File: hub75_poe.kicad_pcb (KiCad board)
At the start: 4 copper layers, 70.5 x 48.3 mm, 103 parts, among them J1 0826-1X1T-JK-F, J2 Conn_02x08_Odd_Even, J3 7466003R, J4 502382-0970, J5 7466003R, Q1 FDS2582, SW1 434133025816, T1 PA2369NL, U1 KSZ8081MLX, U10 SN74LVC8T245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

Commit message: Add transformer snubber diode
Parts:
- added D12: BAS16W, Package_TO_SOT_SMD:SOT-323_SC-70, B.Cu at (131.1, 97.3)
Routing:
- net Net-(D12-Pad1): vias 0 -> 4
- added copper zone on B.Cu, net Net-(D12-Pad1)

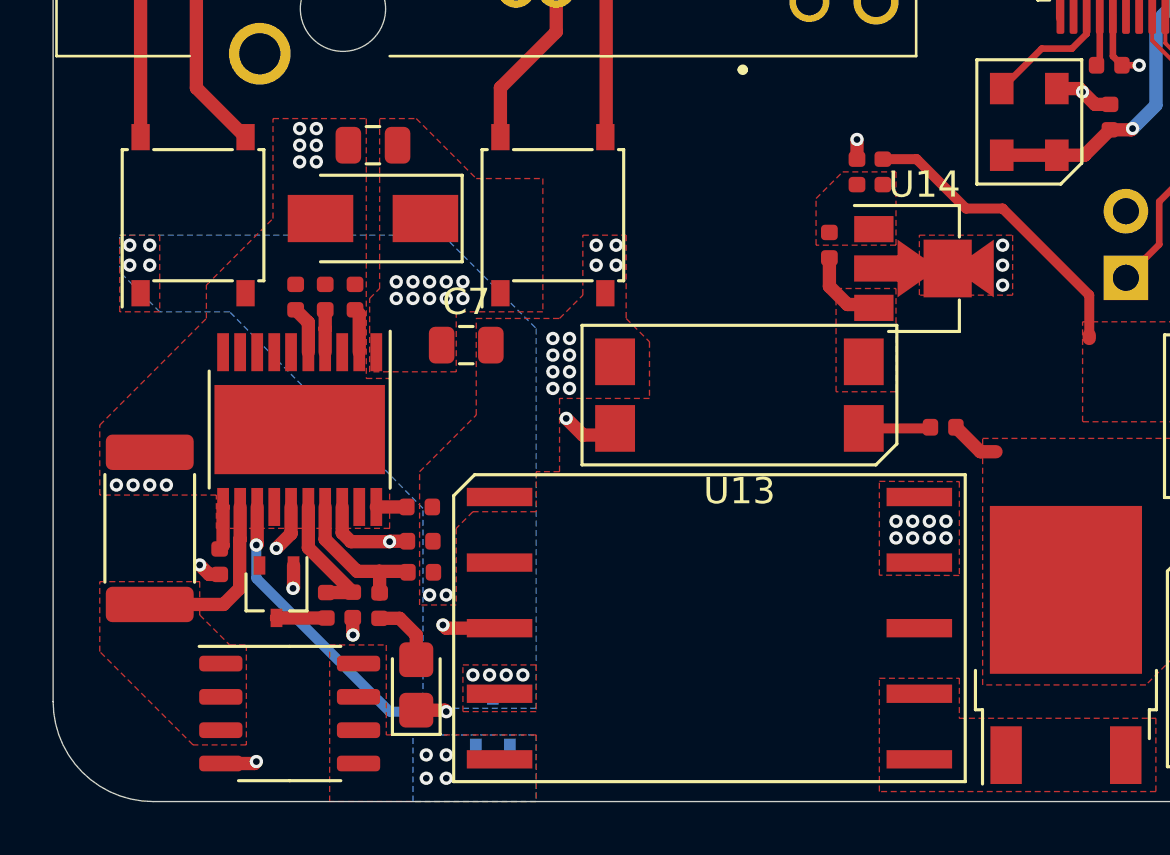
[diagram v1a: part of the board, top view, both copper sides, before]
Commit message: Move snubber diode to board front
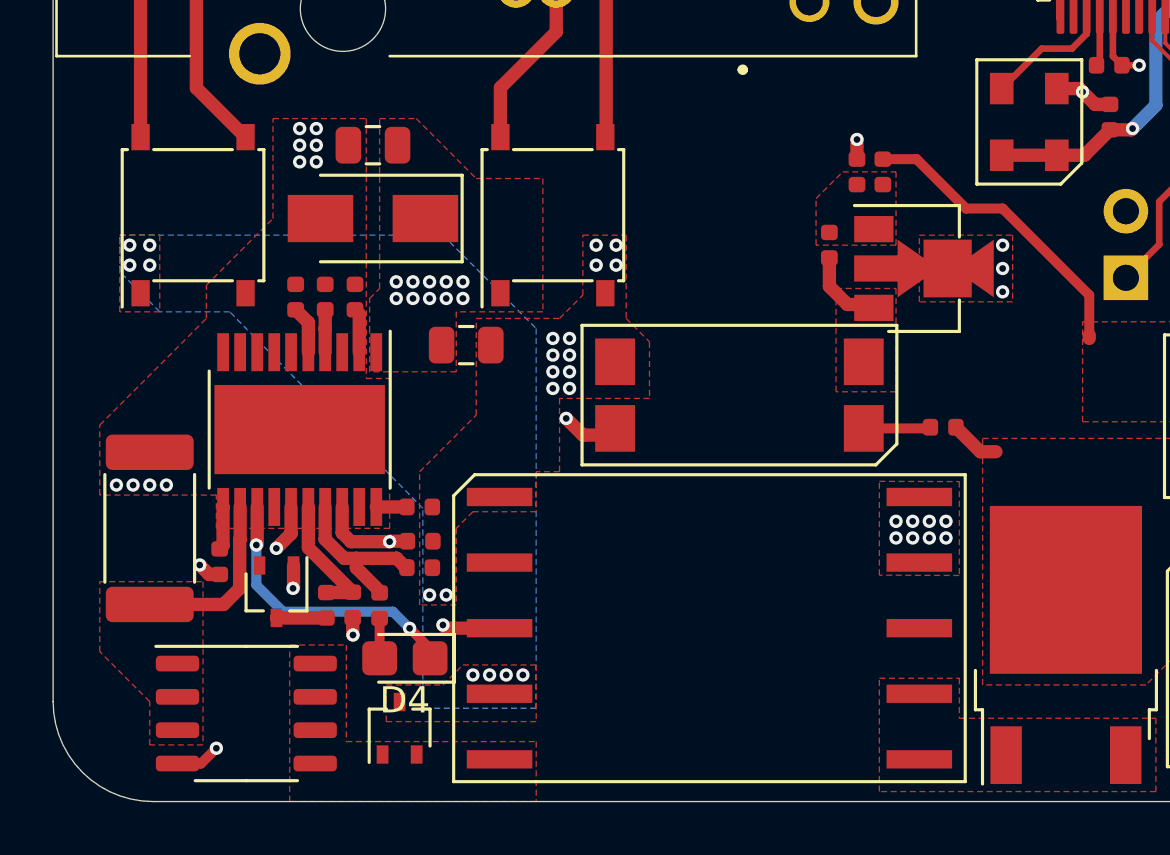
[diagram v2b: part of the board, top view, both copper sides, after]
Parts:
- D12: moved to F.Cu
- moved D12 3.57 mm to (127.5, 97.5)
- moved Q1 1.65 mm to (121.7, 97.0)
- moved D4 1.11 mm to (127.7, 94.9), turned to 180 degrees
- moved C6 0.18 mm to (128.3, 91.4)
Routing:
- net Net-(D4-Pad1): track 13.2 -> 11.0 mm
- net Net-(D4-Pad2): track 2.60 -> 1.52 mm
- net Net-(C6-Pad1): track 5.79 -> 6.53 mm
- net Net-(D12-Pad1): vias 4 -> 0
- removed copper zone on B.Cu, net Net-(D12-Pad1)
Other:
- net class Default removed
- net class HVDC removed

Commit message: Add @dev ref to plot-gerbers step
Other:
- board text added: "PROJECT LIGHTNING PACKET ${GIT_REV} POWER PARTIALLY TESTED"
- board text removed: "PROJECT LIGHTNING PACKET ${GIT_REV} UNTESTED"
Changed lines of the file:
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@@
     (effects (font (size 1.5 1.5) (thickness 0.3)) (justify mirror))
   )
-  (gr_text "PROJECT LIGHTNING PACKET\n${GIT_REV}\nUNTESTED" (at 157.988 86.868) (layer "B.SilkS")
+  (gr_text "PROJECT LIGHTNING PACKET\n${GIT_REV}\nPOWER PARTIALLY TESTED" (at 157.988 86.868) (layer "B.SilkS")
     (effects (font (size 1 1) (thickness 0.15)) (justify mirror))
   )
